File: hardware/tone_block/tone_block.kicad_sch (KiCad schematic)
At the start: 16 parts, among them J1 I/O, Q1 RS32716R

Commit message: Tone block v2
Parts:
- added C5: 4.7uF, Capacitor_SMD:C_0603_1608Metric, symbol Device:C
- added C6: 47uF, Capacitor_SMD:C_0603_1608Metric, symbol Device:C
- added R7, R8: 100k, Resistor_SMD:R_0402_1005Metric, symbol Device:R
- added SW1: SW_SPDT, symbol Switch:SW_SPDT
- added U1: TLV170IDBVR, Package_TO_SOT_SMD:SOT-23-5, symbol cycfi_library:opamp_dbv
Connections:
- net GND: now also R8.2, U1.2 (V-)
- net ext_cap: now also L1.2; no longer J1.10 (Pin_10)
- net in: now also C5.2, SW1.3 (C); no longer L1.1
- net at Q1.C, R1.2: no longer L1.2
- removed net mix: J1.8 (Pin_8), J1.9 (Pin_9), R6.2
- net vcc renamed v+
- net v+: now also R7.1, U1.5 (V+)
- new net: C6.2, U1.1, U1.4 (-)
- new net: C5.1, R7.2, R8.1, U1.3 (+)
- new net out: J1.8 (Pin_8), SW1.2 (B)
- new net res_in: C6.1, L1.1
- new net res_out: R6.2, SW1.1 (A)
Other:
- note added: "1, 2: External capacitor 3, 4, 5: Main input and (pass thru) power 6, 7, 8: Main output and (pass thru) power"
- note added: "Buffer"
- note added: "Bypass Switch"
- note added: "Mounting Holes"
- note removed: "1, 2: External capacitor 3, 4, 5: Main input and (pass thru) power"
- note removed: "6, 7, 8: Main output and (pass thru) power 9, 10: Mixing resistor shunt"
- moved on the sheet: C1, C2, C3, C4, Freq1, H1, H2, J1, L1, Q1, R1, R2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

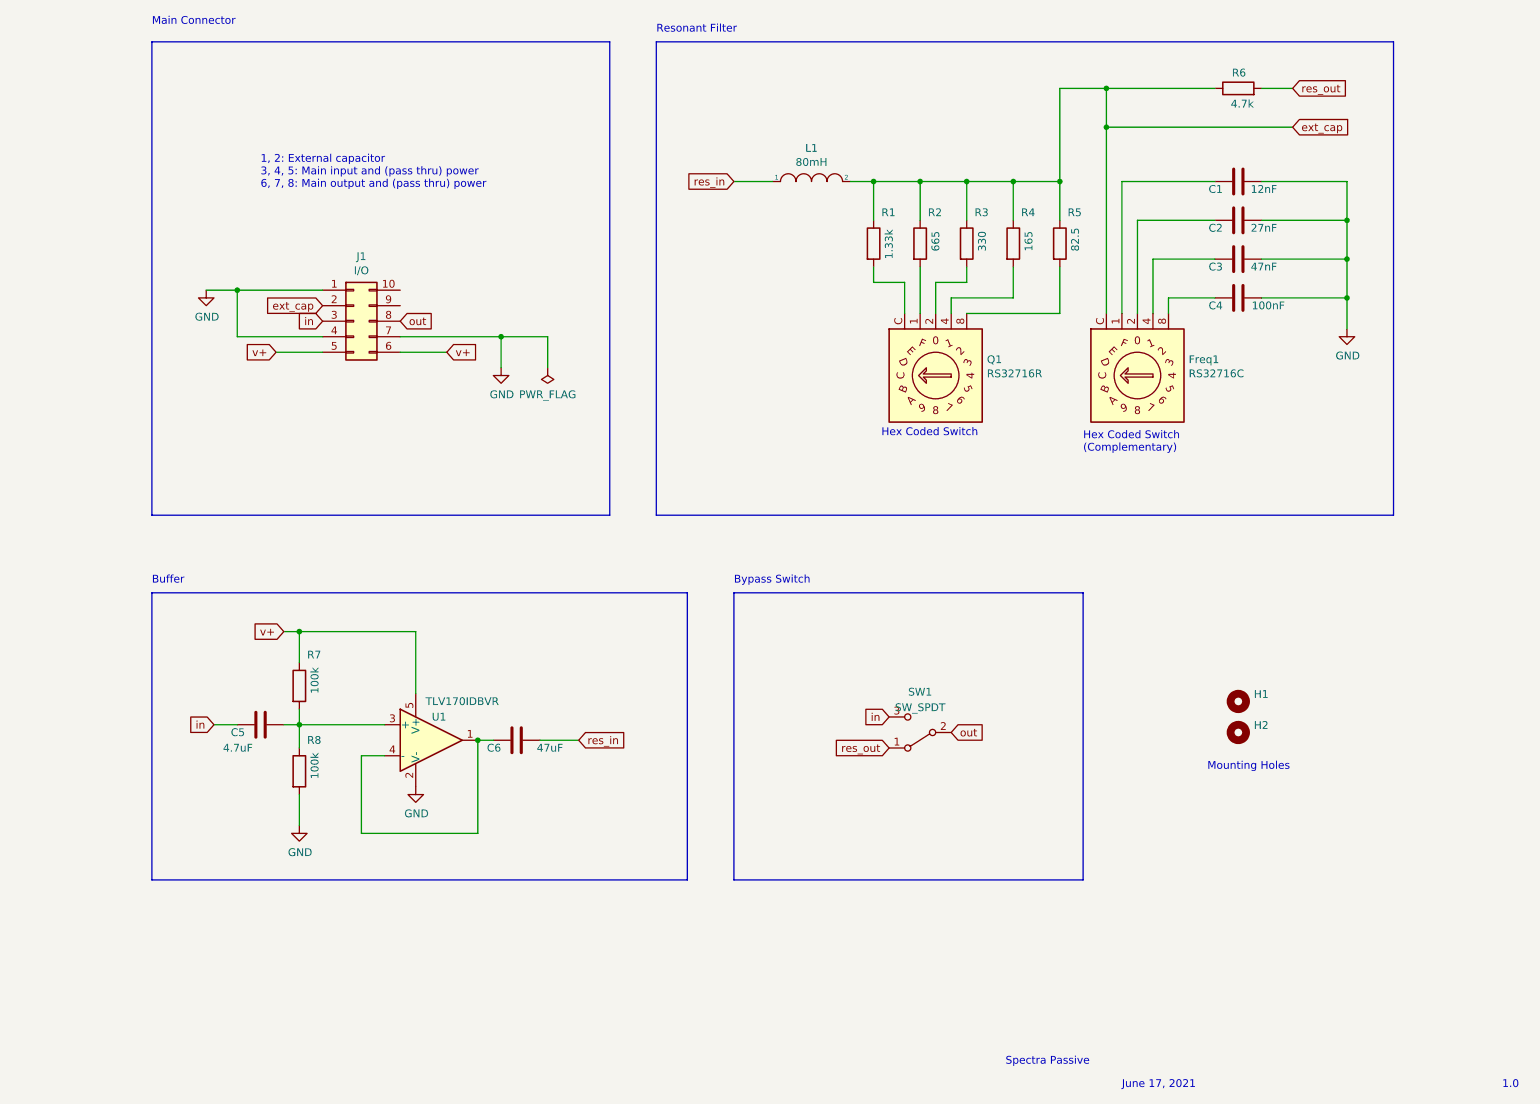
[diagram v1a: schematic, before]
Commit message: Updates to power conditioning section
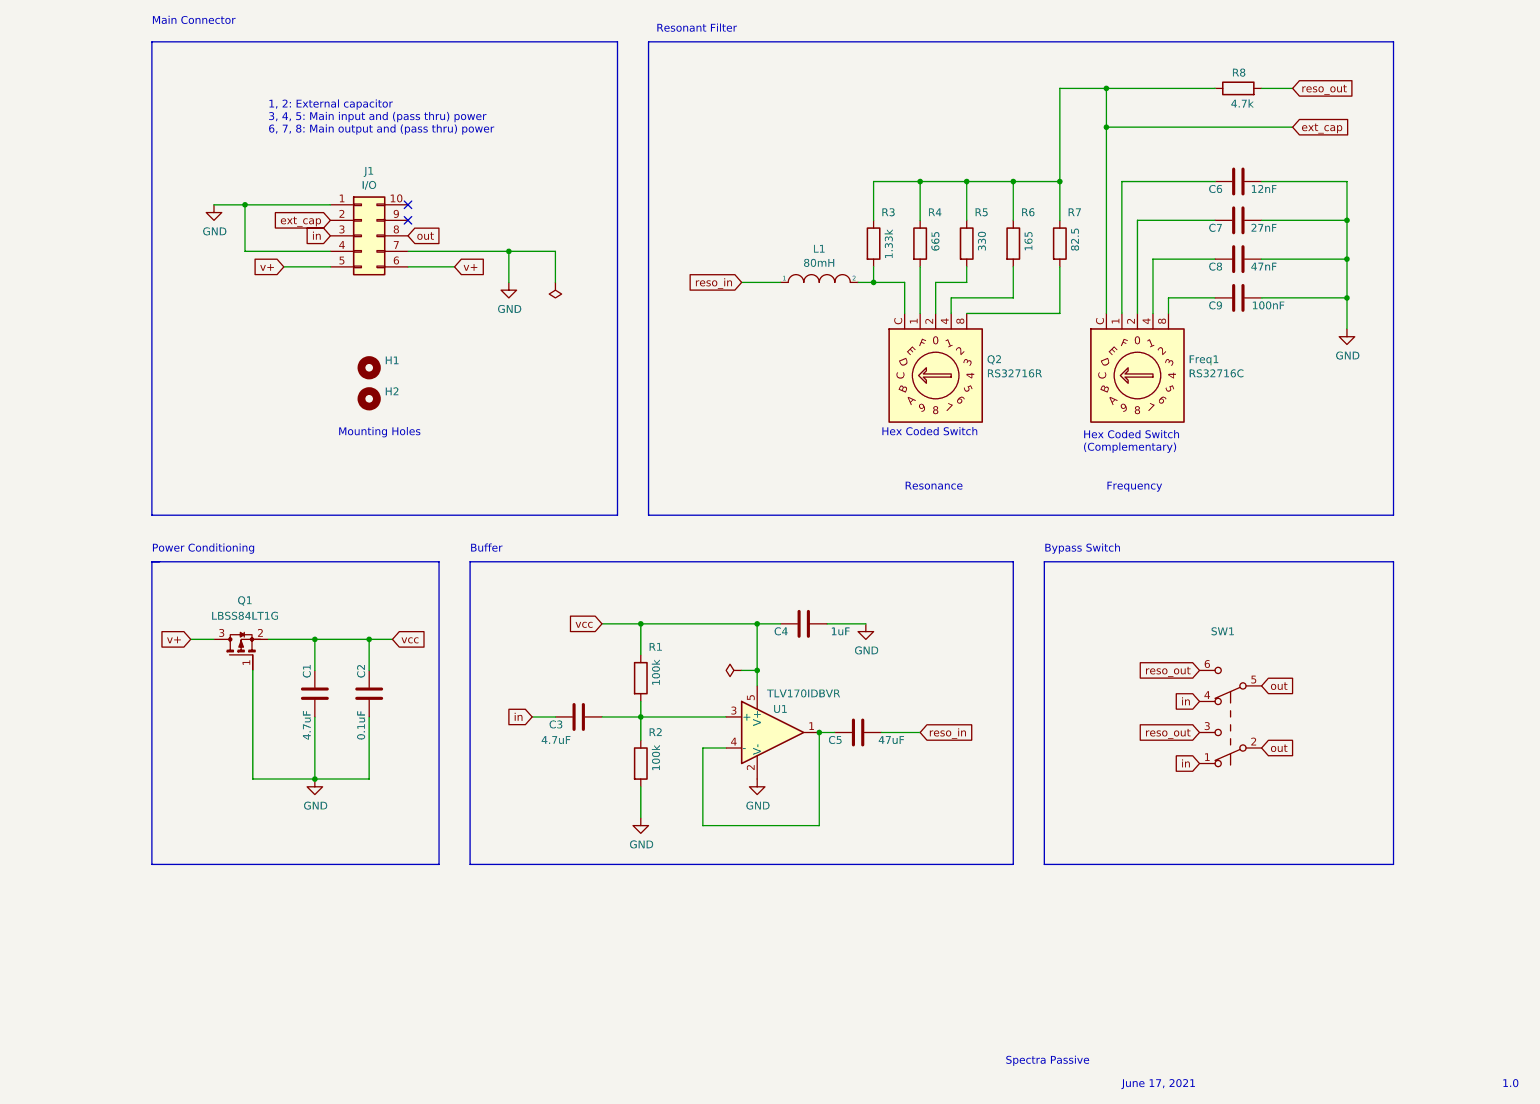
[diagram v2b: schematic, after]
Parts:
- added C1: 4.7uF, Capacitor_SMD:C_0603_1608Metric, symbol Device:C
- added C2: 0.1uF, Capacitor_SMD:C_0402_1005Metric, symbol Device:C
- added C4: 1uF, Capacitor_SMD:C_0402_1005Metric, symbol Device:C
- added Q1: LBSS84LT1G, symbol cycfi_library:q_pmos_gsd
- SW1: value SW_SPDT -> DPDT; symbol Switch:SW_SPDT -> Switch:SW_Push_DPDT
- renumbered C5 to C3, C6 to C5, C1 to C6, C2 to C7, C3 to C8, C4 to C9, Q1 to Q2, R7 to R1, R8 to R2, R1 to R3, R2 to R4, R3 to R5, R4 to R6, R5 to R7, R6 to R8
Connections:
- net GND: now also C1.1, C2.1, C4.1, Q1.1 (G)
- net ext_cap: no longer L1.2
- net in: now also SW1.1 (A), SW1.4 (A); no longer SW1.3 (C)
- net out: now also SW1.5 (B)
- net v+: now also Q1.3 (D); no longer R1.1, U1.5 (V+)
- net at Q2.C, R3.2: now also L1.2
- net res_in renamed reso_in
- net res_out renamed reso_out
- net reso_out: now also SW1.3 (C), SW1.6 (C); no longer SW1.1 (A)
- new net vcc: C1.2, C2.2, C4.2, Q1.2 (S), R1.1, U1.5 (V+)
- no-connect marks 0 -> 2
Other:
- note added: "Frequency"
- note added: "Power Conditioning"
- note added: "Resonance"
- moved on the sheet: C3, C5, H1, H2, J1, L1, R1, R2, U1

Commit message: PCB layout, first take
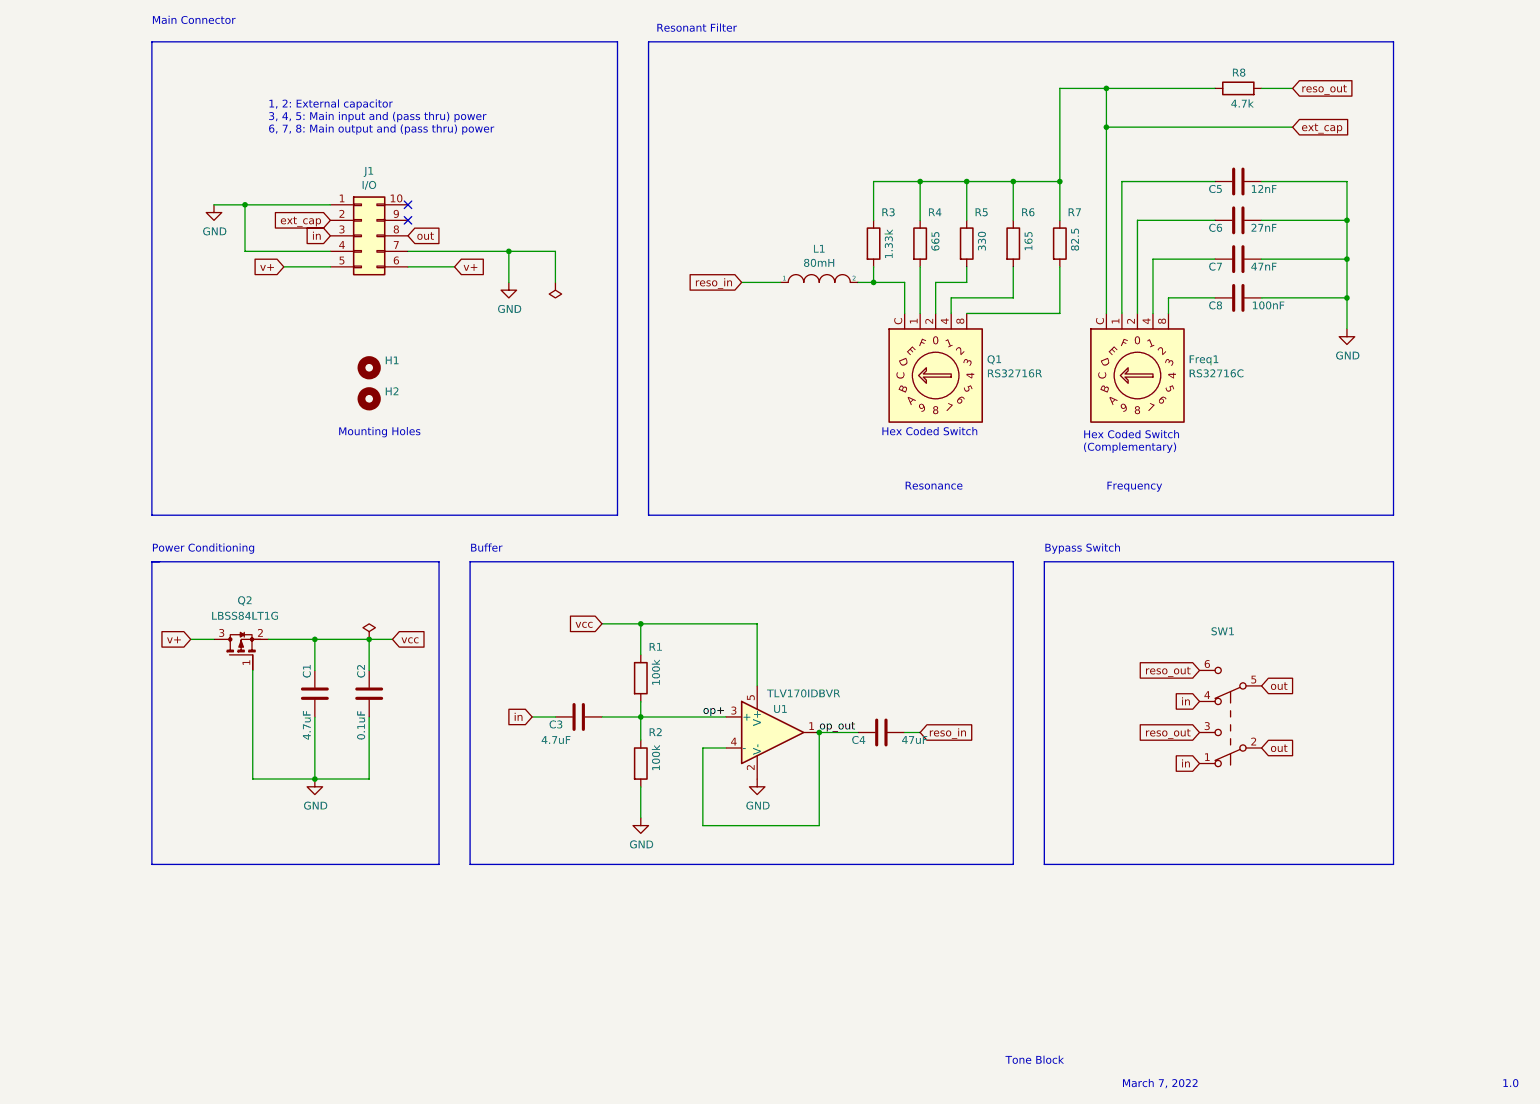
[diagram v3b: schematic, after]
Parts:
- removed C4: 1uF, Capacitor_SMD:C_0402_1005Metric, symbol Device:C
- Q2: renamed from Q1; footprint (none) -> Package_TO_SOT_SMD:SOT-23
- SW1: footprint (none) -> cycfi_library:PS5801
- renumbered C5 to C4, C6 to C5, C7 to C6, C8 to C7, C9 to C8, Q2 to Q1
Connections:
- net op_out: now reaches C4.2, U1.1, U1.4 (-)
- net op+: now reaches C3.1, R1.2, R2.1, U1.3 (+)
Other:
- note added: "March 7, 2022"
- note added: "Tone Block"
- note removed: "June 17, 2021"
- note removed: "Spectra Passive"
- moved on the sheet: C4

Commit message: Using resistor/capacitor network of same values
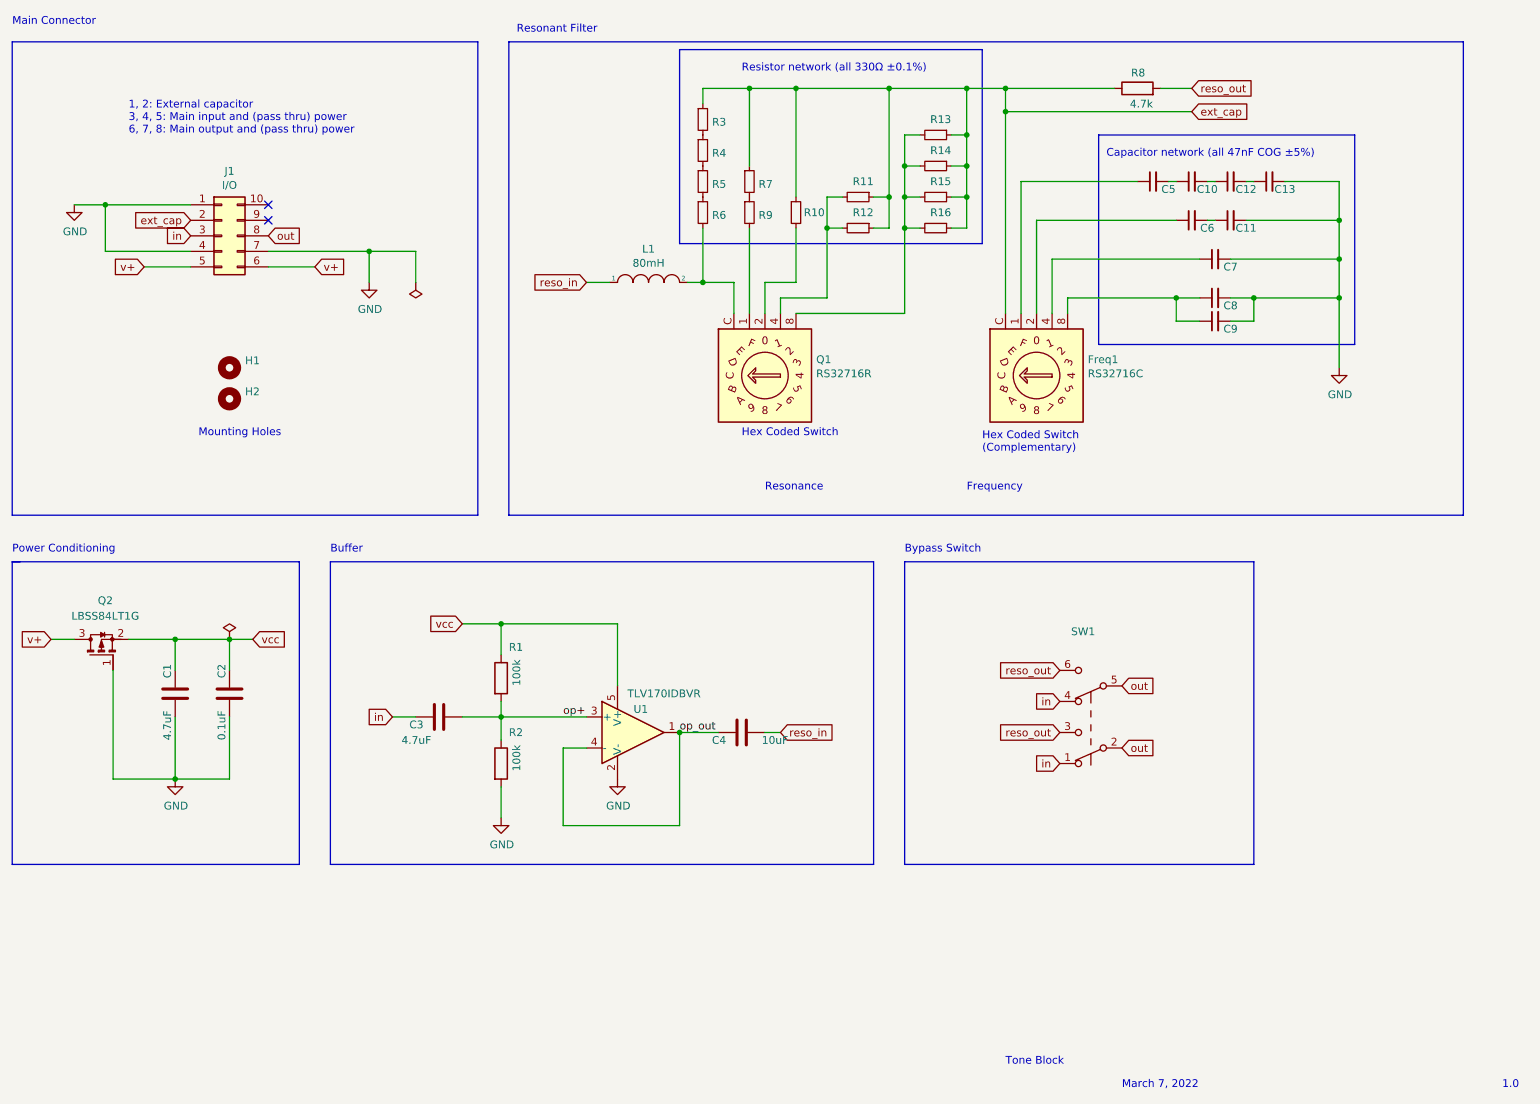
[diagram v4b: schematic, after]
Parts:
- removed C5: 12nF, Capacitor_SMD:C_0402_1005Metric, symbol Device:C
- removed C6: 27nF, Capacitor_SMD:C_0402_1005Metric, symbol Device:C
- removed C7: 47nF, Capacitor_SMD:C_0402_1005Metric, symbol Device:C
- removed C8: 100nF, Capacitor_SMD:C_0402_1005Metric, symbol Device:C
- removed R3: 1.33k, Resistor_SMD:R_0402_1005Metric, symbol Device:R
- removed R4: 665, Resistor_SMD:R_0402_1005Metric, symbol Device:R
- removed R5: 330, Resistor_SMD:R_0402_1005Metric, symbol Device:R
- removed R6: 165, Resistor_SMD:R_0402_1005Metric, symbol Device:R
- removed R7: 82.5, Resistor_SMD:R_0402_1005Metric, symbol Device:R
- added C10, C11, C12, C13, C5, C6, C7, C8, C9: 47nF, Resistor_SMD:R_0402_1005Metric, symbol Device:C_Small
- added R10, R11, R12, R13, R14, R15, R16, R3, R4, R5, R6, R7, R9: 330, Resistor_SMD:R_0402_1005Metric, symbol Device:R_Small
- C4: value 47uF -> 10uF; footprint Capacitor_SMD:C_0603_1608Metric -> Resistor_SMD:R_0603_1608Metric
- J1: footprint cycfi_library:pin_header_2x05_P2.54mm_vertical -> cycfi_library:pin_header_2x5_P2.54mm_vertical
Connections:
- net GND: now also C11.2, C13.2, C7.2, C8.2, C9.2
- net ext_cap: now also R10.1, R11.1, R12.1, R13.1, R14.1, R15.1, R16.1, R3.1, R7.1
- net at L1.2, Q1.C: now also R6.2
- net at Q1.1: now also R9.2
- net at Q1.2: now also R10.2
- net at Q1.4: now also R11.2, R12.2
- net at Q1.8: now also R13.2, R14.2, R15.2, R16.2
- net at Freq1.4: now also C7.1
- net at Freq1.8: now also C8.1, C9.1
- net at Freq1.2: now also C6.1
- net at Freq1.1: now also C5.1
- new net: R3.2, R4.1
- new net: R5.2, R6.1
- new net: C11.1, C6.2
- new net: C12.2, C13.1
- new net: C10.2, C12.1
- new net: R4.2, R5.1
- new net: R7.2, R9.1
- new net: C10.1, C5.2
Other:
- note added: "Capacitor network (all 47nF COG ±5%)"
- note added: "Resistor network (all 330Ω ±0.1%)"
- moved on the sheet: C1, C2, C3, C4, Freq1, H1, H2, J1, L1, Q1, Q2, R1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
